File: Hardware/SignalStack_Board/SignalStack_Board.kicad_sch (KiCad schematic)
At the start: 74 parts, among them J2 RJ45_LED_Shielded, J3 Molex_uF_SV_06, Q1 SI4156DY, Q2 SI4156DY, Q3 SI4156DY, Q4 SI4156DY, Q5 SI4156DY, Q6 SI4156DY, Q7 SI4156DY, Q8 SI4156DY, Q9 Q_PMOS_DGS, SW1 SW_Push, SW2 SW_Push, U1 OKI, U10 74LVC2G04, U2 SMAJ12CA, U3 Teensy4.1_DEV-16771, U4 TSR_1-2450, U5 IRS2005S, U6 IRS2005S, U7 74LVC2G04, U8 IRS2005S, U9 IRS2005S

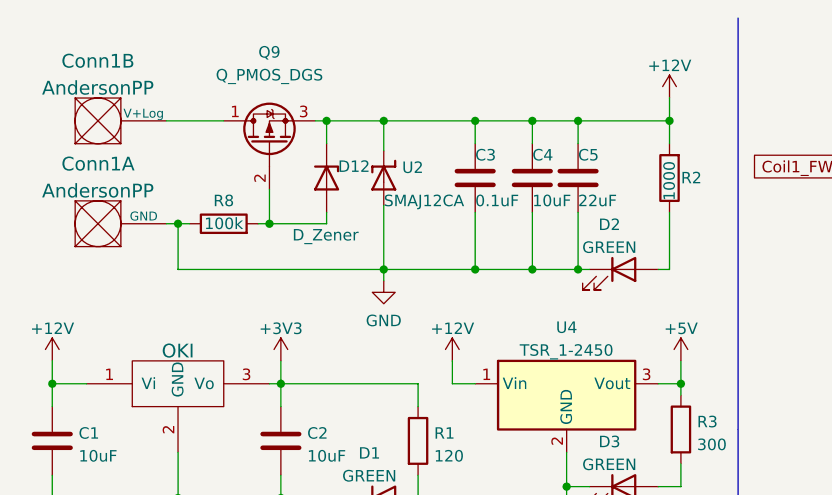
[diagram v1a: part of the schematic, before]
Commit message: Mostly finished H bridges
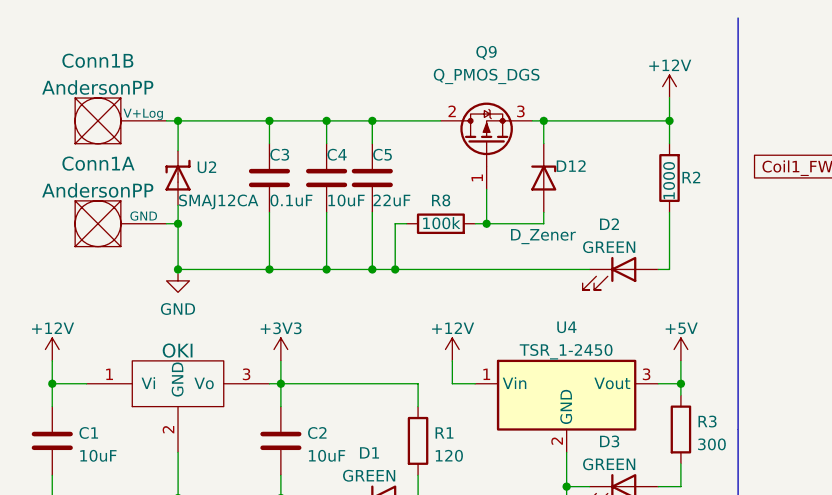
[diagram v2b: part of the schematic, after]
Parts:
- Q9: symbol Device:Q_PMOS_DGS -> Device:Q_PMOS_GDS
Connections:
- net +12V: no longer C3.1, C4.1, C5.1, U2.C
- net at Conn1.2 (V+Log): now also C3.1, C4.1, C5.1, Q9.2 (D), U2.C; no longer Q9.1 (D)
- net at D12.2 (A), R8.2: now also Q9.1 (G); no longer Q9.2 (G)
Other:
- moved on the sheet: C3, C4, C5, D12, Q9, R8, U2

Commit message: Finished layout
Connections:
- net Coil1_FWD: now also U3.12 (MISO); no longer U3.14 (A0)
- net Coil1_RVS: now also U3.11 (MOSI); no longer U3.15 (A1)
- net Coil2_FWD: now also U3.29 (TX7); no longer U3.22 (A8)
- net Coil2_RVS: now also U3.28 (RX7); no longer U3.23 (A9)
- net GPS RX: now also U3.34 (RX8); no longer U3.0 (RX1)
- net GPS TX: now also U3.35 (TX8); no longer U3.1 (TX1)
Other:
- moved on the sheet: U3

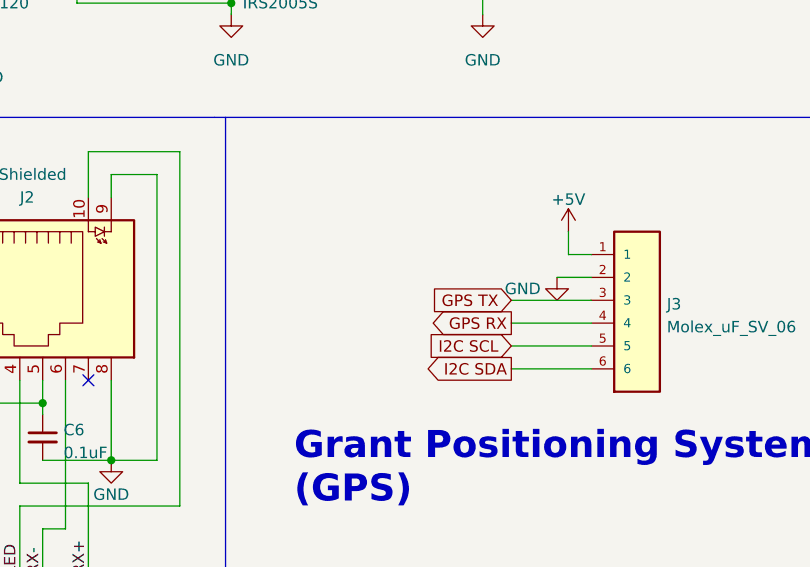
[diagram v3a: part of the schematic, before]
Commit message: Added pull up resistors
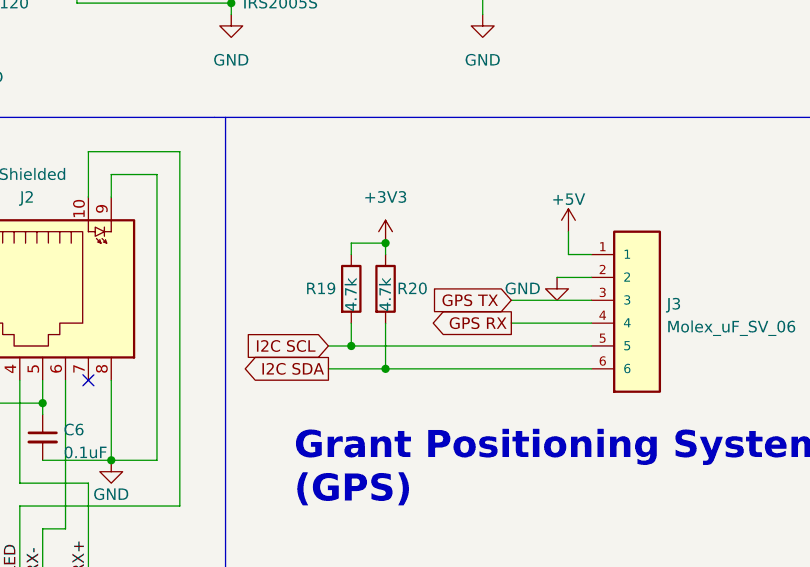
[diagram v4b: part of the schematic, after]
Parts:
- added R19, R20: 4.7k, Resistor_SMD:R_0603_1608Metric_Pad0.98x0.95mm_HandSolder, symbol Device:R
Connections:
- net +3V3: now also R19.1, R20.1
- net I2C SCL: now also R19.2
- net I2C SDA: now also R20.2
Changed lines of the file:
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@@
   (junction (at 45.72 39.37) (diameter 0) (color 0 0 0 0)
   )
+  (junction (at 151.13 139.7) (diameter 0) (color 0 0 0 0)
+  )
   (junction (at 227.33 132.08) (diameter 0) (color 0 0 0 0)
   )
@@
   (junction (at 50.8 39.37) (diameter 0) (color 0 0 0 0)
   )
+  (junction (at 151.13 125.73) (diameter 0) (color 0 0 0 0)
+  )
   (junction (at 245.745 48.26) (diameter 0) (color 0 0 0 0)
   )
@@
   (junction (at 71.12 184.15) (diameter 0) (color 0 0 0 0)
   )
+  (junction (at 147.32 137.16) (diameter 0) (color 0 0 0 0)
+  )
   (junction (at 212.09 121.92) (diameter 0) (color 0 0 0 0)
   )
@@
     (stroke (width 0) (type default) (color 0 0 0 0))
   )
+  (wire (pts (xy 147.32 125.73) (xy 151.13 125.73))
+    (stroke (width 0) (type default) (color 0 0 0 0))
+  )
   (wire (pts (xy 262.89 90.17) (xy 262.89 99.06))
     (stroke (width 0) (type default) (color 0 0 0 0))
@@
     (stroke (width 0) (type default) (color 0 0 0 0))
   )
+  (wire (pts (xy 151.13 125.73) (xy 151.13 127))
+    (stroke (width 0) (type default) (color 0 0 0 0))
+  )
   (wire (pts (xy 68.58 100.33) (xy 83.82 100.33))
     (stroke (width 0) (type default) (color 0 0 0 0))
@@
     (stroke (width 0) (type default) (color 0 0 0 0))
   )
+  (wire (pts (xy 151.13 139.7) (xy 173.99 139.7))
+    (stroke (width 0) (type default) (color 0 0 0 0))
+  )
+  (wire (pts (xy 151.13 134.62) (xy 151.13 139.7))
+    (stroke (width 0) (type default) (color 0 0 0 0))
+  )
   (wire (pts (xy 225.425 35.56) (xy 217.805 35.56))
     (stroke (width 0) (type default) (color 0 0 0 0))
@@
     (stroke (width 0) (type default) (color 0 0 0 0))
   )
+  (wire (pts (xy 147.32 127) (xy 147.32 125.73))
+    (stroke (width 0) (type default) (color 0 0 0 0))
+  )
   (wire (pts (xy 106.68 101.6) (xy 106.68 102.87))
     (stroke (width 0) (type default) (color 0 0 0 0))
@@
     (stroke (width 0) (type default) (color 0 0 0 0))
   )
-  (wire (pts (xy 165.1 137.16) (xy 173.99 137.16))
+  (wire (pts (xy 144.78 137.16) (xy 147.32 137.16))
     (stroke (width 0) (type default) (color 0 0 0 0))
   )
@@
     (stroke (width 0) (type default) (color 0 0 0 0))
   )
+  (wire (pts (xy 147.32 134.62) (xy 147.32 137.16))
+    (stroke (width 0) (type default) (color 0 0 0 0))
+  )
   (wire (pts (xy 113.03 149.86) (xy 120.65 149.86))
     (stroke (width 0) (type default) (color 0 0 0 0))
@@
     (stroke (width 0) (type default) (color 0 0 0 0))
   )
-  (wire (pts (xy 165.1 139.7) (xy 173.99 139.7))
+  (wire (pts (xy 144.78 139.7) (xy 151.13 139.7))
+    (stroke (width 0) (type default) (color 0 0 0 0))
+  )
+  (wire (pts (xy 147.32 137.16) (xy 173.99 137.16))
     (stroke (width 0) (type default) (color 0 0 0 0))
   )
@@
     )
   )
-  (global_label "I2C SCL" (shape input) (at 165.1 137.16 180) (fields_autoplaced)
+  (global_label "I2C SCL" (shape input) (at 144.78 137.16 180) (fields_autoplaced)
     (effects (font (size 1.27 1.27)) (justify right))
-    (property "Intersheet References" "${INTERSHEET_REFS}" (id 0) (at 155.1274 137.0806 0)
+    (property "Intersheet References" "${INTERSHEET_REFS}" (id 0) (at 134.8074 137.0806 0)
       (effects (font (size 1.27 1.27)) (justify right) hide)
     )
@@
     )
   )
-  (global_label "I2C SDA" (shape output) (at 165.1 139.7 180) (fields_autoplaced)
+  (global_label "I2C SDA" (shape output) (at 144.78 139.7 180) (fields_autoplaced)
     (effects (font (size 1.27 1.27)) (justify right))
-    (property "Intersheet References" "${INTERSHEET_REFS}" (id 0) (at 155.0669 139.6206 0)
+    (property "Intersheet References" "${INTERSHEET_REFS}" (id 0) (at 134.7469 139.6206 0)
       (effects (font (size 1.27 1.27)) (justify right) hide)
     )
@@
     (pin "2")
   )
+  (symbol (lib_name "+3V3_2") (lib_id "power:+3V3") (at 151.13 125.73 0) (unit 1)
+    (in_bom yes) (on_board yes) (fields_autoplaced)
+    (property "Reference" "#PWR041" (id 0) (at 151.13 129.54 0)
+      (effects (font (size 1.27 1.27)) hide)
+    )
+    (property "Value" "+3V3" (id 1) (at 151.13 120.65 0))
+    (property "Footprint" "" (id 2) (at 151.13 125.73 0)
+      (effects (font (size 1.27 1.27)) hide)
+    )
+    (property "Datasheet" "" (id 3) (at 151.13 125.73 0)
+      (effects (font (size 1.27 1.27)) hide)
+    )
+    (pin "1")
+  )
   (symbol (lib_id "power:+12V") (at 15.24 49.53 0) (unit 1)
     (in_bom yes) (on_board yes) (fields_autoplaced)
@@
     (pin "2")
   )
+  (symbol (lib_id "Device:R") (at 147.32 130.81 0) (unit 1)
+    (in_bom yes) (on_board yes)
+    (property "Reference" "R19" (id 0) (at 142.24 130.81 0)
+      (effects (font (size 1.27 1.27)) (justify left))
+    )
+    (property "Value" "4.7k" (id 1) (at 147.32 133.35 90)
+      (effects (font (size 1.27 1.27)) (justify left))
+    )
+    (property "Footprint" "Resistor_SMD:R_0603_1608Metric_Pad0.98x0.95mm_HandSolder" (id 2) (at 145.542 130.81 90)
+      (effects (font (size 1.27 1.27)) hide)
+    )
+    (property "Datasheet" "~" (id 3) (at 147.32 130.81 0)
+      (effects (font (size 1.27 1.27)) hide)
+    )
+    (pin "1")
+    (pin "2")
+  )
   (symbol (lib_id "Driver_FET:IRS2005S") (at 245.745 85.09 0) (mirror y) (unit 1)
     (in_bom yes) (on_board yes)
@@
     (pin "1")
   )
+  (symbol (lib_id "Device:R") (at 151.13 130.81 0) (unit 1)
+    (in_bom yes) (on_board yes)
+    (property "Reference" "R20" (id 0) (at 152.4 130.81 0)
+      (effects (font (size 1.27 1.27)) (justify left))
+    )
+    (property "Value" "4.7k" (id 1) (at 151.13 133.35 90)
+      (effects (font (size 1.27 1.27)) (justify left))
+    )
+    (property "Footprint" "Resistor_SMD:R_0603_1608Metric_Pad0.98x0.95mm_HandSolder" (id 2) (at 149.352 130.81 90)
+      (effects (font (size 1.27 1.27)) hide)
+    )
+    (property "Datasheet" "~" (id 3) (at 151.13 130.81 0)
+      (effects (font (size 1.27 1.27)) hide)
+    )
+    (pin "1")
+    (pin "2")
+  )
   (symbol (lib_id "Transistor_FET:FDS2734") (at 220.345 41.91 0) (mirror y) (unit 1)
     (in_bom yes) (on_board yes)
@@
       (reference "#PWR040") (unit 1) (value "GND") (footprint "")
     )
+    (path "/2644c039-4585-491f-95a4-bf76300b1d70"
+      (reference "#PWR041") (unit 1) (value "+3V3") (footprint "")
+    )
     (path "/5e643a67-3a40-4e53-aae3-f84d056d6470"
       (reference "C1") (unit 1) (value "10uF") (footprint "Capacitor_SMD:C_0603_1608Metric_Pad1.08x0.95mm_HandSolder")
@@
       (reference "R18") (unit 1) (value "120") (footprint "Resistor_SMD:R_0603_1608Metric_Pad0.98x0.95mm_HandSolder")
     )
+    (path "/3a046731-6f4f-46fe-813d-f26828f92785"
+      (reference "R19") (unit 1) (value "4.7k") (footprint "Resistor_SMD:R_0603_1608Metric_Pad0.98x0.95mm_HandSolder")
+    )
+    (path "/88e3236a-62e2-4cd9-a681-6c76acbf5e11"
+      (reference "R20") (unit 1) (value "4.7k") (footprint "Resistor_SMD:R_0603_1608Metric_Pad0.98x0.95mm_HandSolder")
+    )
     (path "/c2c95523-d3ad-44d2-896c-c965a1899e77"

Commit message: Rev3 schematic
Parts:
- removed C6: 0.1uF, Capacitor_SMD:C_0603_1608Metric_Pad1.08x0.95mm_HandSolder, symbol Device:C_Small
- removed J2: RJ45_LED_Shielded, MRDT_Connectors:RJ45_Teensy, symbol Connector:RJ45_LED_Shielded
- removed J3: Molex_uF_SV_06, Connector_Molex:Molex_SL_171971-0006_1x06_P2.54mm_Vertical, symbol MRDT_Connectors:Molex_uF_SV_06
- removed R19, R20: 4.7k, Resistor_SMD:R_0603_1608Metric_Pad0.98x0.95mm_HandSolder, symbol Device:R
- removed U2: SMAJ12CA, MRDT_Actives:DO-214AC, symbol SMAJ12CA:SMAJ12CA
- removed U3: Teensy4.1_DEV-16771, MRDT_Shields:Teensy_4_1_Ethernet, symbol MRDT_Shields:Teensy4.1_DEV-16771
- added A?: Arduino_UNO_R3, Module:Arduino_UNO_R3, symbol MCU_Module:Arduino_UNO_R3
- added U?: Raspberry_Pi, symbol MRDT_Shields:Raspberry_Pi
- C3: value 0.1uF -> 100uF; symbol Device:C -> Device:C_Polarized
- C4: value 10uF -> 220uF; symbol Device:C -> Device:C_Polarized
- C5: value 22uF -> 470uF; symbol Device:C -> Device:C_Polarized
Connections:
- net +12V: now also C3.1, C4.1, C5.1
- net +3V3: now also A?.2 (IOREF)
- net +5V: now also A?.5 (+5V), U?.2 (+5V), U?.4 (+5V)
- net Coil1_FWD: now also U?.32 (GP_12)
- net Coil1_RVS: now also U?.33 (GP_13)
- net Coil2_FWD: now also U?.12 (GP_18)
- net Coil2_RVS: now also U?.35 (GP_19)
- net GND: now also A?.29 (GND), A?.6 (GND), A?.7 (GND), U?.14 (GND), U?.20 (GND), U?.25 (GND), U?.30 (GND), U?.34 (GND), U?.39 (GND), U?.6 (GND), U?.9 (GND)
- net Motor 1: now also U?.15 (GP_22)
- net Motor 2: now also U?.16 (GP_24)
- new net: Conn1.2 (V+Log), Q9.2 (D)
- new net GPS_RX1: A?.17 (D2), U?.8 (GP_14)
- new net GPS_TX1: A?.23 (D8), U?.10 (GP_15)
- no-connect marks 43 -> 46
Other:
- note removed: "Ethernet"
- note removed: "Grant Positioning System (GPS)"
- note removed: "Teensy"
- moved on the sheet: D12, D13, D14, Q9, R13, R18, R8, SW1, SW2, V1, V2, V3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

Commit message: Made Rev3 layout
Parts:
- removed V4: Via, MRDT_Drill_Holes:4_40_Hole_Corner, symbol MRDT_Drill_Holes:Via
- C3, C4: footprint Capacitor_SMD:C_0603_1608Metric_Pad1.08x0.95mm_HandSolder -> Capacitor_THT:CP_Radial_D6.3mm_P2.50mm
- C5: footprint Capacitor_SMD:C_0603_1608Metric_Pad1.08x0.95mm_HandSolder -> Capacitor_THT:CP_Radial_D10.0mm_P2.50mm
- U2: renamed from U?; footprint (none) -> MRDT_Shields:RaspberryPi_THT_BOTTOM
- gave numbers to parts that had none: 1
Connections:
- net Coil1_RVS: now also U2.12 (GP_18); no longer U2.33 (GP_13)
- net Coil2_FWD: now also U2.35 (GP_19); no longer U2.12 (GP_18)
- net Coil2_RVS: now also U2.33 (GP_13); no longer U2.35 (GP_19)
